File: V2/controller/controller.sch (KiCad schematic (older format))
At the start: 27 parts, among them J0 Molex_PSU_F, J1 4pins_jumper, J2 Flat_7seg_F, J3 Flat_Rpi_Data_F, Q0 BD139-16, Q1 BD139-16, Q2 BD139-16, Q3 BD139-16, Q4 BD139-16, Q5 BD139-16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

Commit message: Solving ERC
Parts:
- removed J0: Molex_PSU_F, symbol Connector:Conn_01x04_Female
- removed J2: Flat_7seg_F, symbol Connector:Conn_01x08_Female
- removed J3: Flat_Rpi_Data_F, symbol Connector:Conn_01x06_Female
- added D0: 1N4007, symbol Device:D
- added J0: Molex_PSU_F, symbol Connector_Generic:Conn_01x04
- added J2: Flat_7seg_F, symbol Connector_Generic:Conn_02x04_Counter_Clockwise
- added J3: Rpi_DATA_F, symbol Connector_Generic:Conn_02x03_Counter_Clockwise
- D1: value LED_RED -> LED_2V_20mA
- R1: value R -> 100R
- gave numbers to parts that had none: 1
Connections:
- net labels added: Earth
- wire segments 122 -> 135
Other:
- moved on the sheet: D1, R1, R10, R11, R12, R13, R9

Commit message: Identify control pins
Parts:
- R1: value 100R -> 150R
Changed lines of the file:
@@
 P 3850 1450
 F 0 "R1" H 3920 1496 50  0000 L CNN
-F 1 "100R" H 3920 1405 50  0000 L CNN
+F 1 "150R" H 3920 1405 50  0000 L CNN
 F 2 "" V 3780 1450 50  0001 C CNN
 F 3 "~" H 3850 1450 50  0001 C CNN

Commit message: Assign footprints
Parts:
- D0: footprint (none) -> Diode_THT:D_A-405_P10.16mm_Horizontal
- D1: footprint (none) -> LED_THT:LED_D5.0mm
- J0: footprint (none) -> PSU:conn_hdd_15-24-4441
- J1: footprint (none) -> Connector_PinHeader_2.00mm:PinHeader_2x02_P2.00mm_Vertical
- J2: footprint (none) -> Connector_PinHeader_2.54mm:PinHeader_2x04_P2.54mm_Horizontal
- J3: footprint (none) -> Connector_PinHeader_2.54mm:PinHeader_2x03_P2.54mm_Horizontal
- Q0, Q1, Q2, Q3, Q4, Q5, Q6: footprint (none) -> Package_TO_SOT_THT:TO-126-3_Vertical
- R0, R1, R10, R11, R12, R13, R2, R3, R4, R5, R6, R7, R8, R9: footprint (none) -> Resistor_THT:R_Axial_DIN0207_L6.3mm_D2.5mm_P10.16mm_Horizontal
- U1: footprint (none) -> Package_DIP:DIP-16_W7.62mm_LongPads
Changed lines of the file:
@@
 F 0 "Q0" H 6991 1596 50  0000 L CNN
 F 1 "BD139-16" H 6991 1505 50  0000 L CNN
-F 2 "" H 7000 1650 50  0001 C CNN
+F 2 "Package_TO_SOT_THT:TO-126-3_Vertical" H 7000 1650 50  0001 C CNN
 F 3 "~" H 6800 1550 50  0001 C CNN
 	1    6800 1550
@@
 F 0 "R1" H 3920 1496 50  0000 L CNN
 F 1 "150R" H 3920 1405 50  0000 L CNN
-F 2 "" V 3780 1450 50  0001 C CNN
+F 2 "Resistor_THT:R_Axial_DIN0207_L6.3mm_D2.5mm_P10.16mm_Horizontal" V 3780 1450 50  0001 C CNN
 F 3 "~" H 3850 1450 50  0001 C CNN
 	1    3850 1450
@@
 F 0 "D1" V 3439 1332 50  0000 R CNN
 F 1 "LED_2V_20mA" V 3348 1332 50  0000 R CNN
-F 2 "" H 3400 1450 50  0001 C CNN
+F 2 "LED_THT:LED_D5.0mm" H 3400 1450 50  0001 C CNN
 F 3 "~" H 3400 1450 50  0001 C CNN
 	1    3400 1450
@@
 F 0 "R2" H 6320 2096 50  0000 L CNN
 F 1 "430R" H 6320 2005 50  0000 L CNN
-F 2 "" V 6180 2050 50  0001 C CNN
+F 2 "Resistor_THT:R_Axial_DIN0207_L6.3mm_D2.5mm_P10.16mm_Horizontal" V 6180 2050 50  0001 C CNN
 F 3 "~" H 6250 2050 50  0001 C CNN
 	1    6250 2050
@@
 F 0 "R0" H 6320 1596 50  0000 L CNN
 F 1 "430R" H 6320 1505 50  0000 L CNN
-F 2 "" V 6180 1550 50  0001 C CNN
+F 2 "Resistor_THT:R_Axial_DIN0207_L6.3mm_D2.5mm_P10.16mm_Horizontal" V 6180 1550 50  0001 C CNN
 F 3 "~" H 6250 1550 50  0001 C CNN
 	1    6250 1550
@@
 F 0 "Q1" H 6991 2096 50  0000 L CNN
 F 1 "BD139-16" H 6991 2005 50  0000 L CNN
-F 2 "" H 7000 2150 50  0001 C CNN
+F 2 "Package_TO_SOT_THT:TO-126-3_Vertical" H 7000 2150 50  0001 C CNN
 F 3 "~" H 6800 2050 50  0001 C CNN
 	1    6800 2050
@@
 F 0 "Q2" H 6991 2596 50  0000 L CNN
 F 1 "BD139-16" H 6991 2505 50  0000 L CNN
-F 2 "" H 7000 2650 50  0001 C CNN
+F 2 "Package_TO_SOT_THT:TO-126-3_Vertical" H 7000 2650 50  0001 C CNN
 F 3 "~" H 6800 2550 50  0001 C CNN
 	1    6800 2550
@@
 F 0 "Q3" H 6991 3096 50  0000 L CNN
 F 1 "BD139-16" H 6991 3005 50  0000 L CNN
-F 2 "" H 7000 3150 50  0001 C CNN
+F 2 "Package_TO_SOT_THT:TO-126-3_Vertical" H 7000 3150 50  0001 C CNN
 F 3 "~" H 6800 3050 50  0001 C CNN
 	1    6800 3050
@@
 F 0 "Q4" H 6991 3596 50  0000 L CNN
 F 1 "BD139-16" H 6991 3505 50  0000 L CNN
-F 2 "" H 7000 3650 50  0001 C CNN
+F 2 "Package_TO_SOT_THT:TO-126-3_Vertical" H 7000 3650 50  0001 C CNN
 F 3 "~" H 6800 3550 50  0001 C CNN
 	1    6800 3550
@@
 F 0 "Q5" H 6991 4096 50  0000 L CNN
 F 1 "BD139-16" H 6991 4005 50  0000 L CNN
-F 2 "" H 7000 4150 50  0001 C CNN
+F 2 "Package_TO_SOT_THT:TO-126-3_Vertical" H 7000 4150 50  0001 C CNN
 F 3 "~" H 6800 4050 50  0001 C CNN
 	1    6800 4050
@@
 F 0 "Q6" H 6991 4596 50  0000 L CNN
 F 1 "BD139-16" H 6991 4505 50  0000 L CNN
-F 2 "" H 7000 4650 50  0001 C CNN
+F 2 "Package_TO_SOT_THT:TO-126-3_Vertical" H 7000 4650 50  0001 C CNN
 F 3 "~" H 6800 4550 50  0001 C CNN
 	1    6800 4550
@@
 F 0 "R3" H 6320 2596 50  0000 L CNN
 F 1 "430R" H 6320 2505 50  0000 L CNN
-F 2 "" V 6180 2550 50  0001 C CNN
+F 2 "Resistor_THT:R_Axial_DIN0207_L6.3mm_D2.5mm_P10.16mm_Horizontal" V 6180 2550 50  0001 C CNN
 F 3 "~" H 6250 2550 50  0001 C CNN
 	1    6250 2550
@@
 F 0 "R4" H 6320 3096 50  0000 L CNN
 F 1 "430R" H 6320 3005 50  0000 L CNN
-F 2 "" V 6180 3050 50  0001 C CNN
+F 2 "Resistor_THT:R_Axial_DIN0207_L6.3mm_D2.5mm_P10.16mm_Horizontal" V 6180 3050 50  0001 C CNN
 F 3 "~" H 6250 3050 50  0001 C CNN
 	1    6250 3050
@@
 F 0 "R5" H 6320 3596 50  0000 L CNN
 F 1 "430R" H 6320 3505 50  0000 L CNN
-F 2 "" V 6180 3550 50  0001 C CNN
+F 2 "Resistor_THT:R_Axial_DIN0207_L6.3mm_D2.5mm_P10.16mm_Horizontal" V 6180 3550 50  0001 C CNN
 F 3 "~" H 6250 3550 50  0001 C CNN
 	1    6250 3550
@@
 F 0 "R6" H 6320 4096 50  0000 L CNN
 F 1 "430R" H 6320 4005 50  0000 L CNN
-F 2 "" V 6180 4050 50  0001 C CNN
+F 2 "Resistor_THT:R_Axial_DIN0207_L6.3mm_D2.5mm_P10.16mm_Horizontal" V 6180 4050 50  0001 C CNN
 F 3 "~" H 6250 4050 50  0001 C CNN
 	1    6250 4050
@@
 F 0 "R7" H 6320 4596 50  0000 L CNN
 F 1 "430R" H 6320 4505 50  0000 L CNN
-F 2 "" V 6180 4550 50  0001 C CNN
+F 2 "Resistor_THT:R_Axial_DIN0207_L6.3mm_D2.5mm_P10.16mm_Horizontal" V 6180 4550 50  0001 C CNN
 F 3 "~" H 6250 4550 50  0001 C CNN
 	1    6250 4550
@@
 F 0 "R8" H 4320 1596 50  0000 L CNN
 F 1 "1k" H 4320 1505 50  0000 L CNN
-F 2 "" V 4180 1550 50  0001 C CNN
+F 2 "Resistor_THT:R_Axial_DIN0207_L6.3mm_D2.5mm_P10.16mm_Horizontal" V 4180 1550 50  0001 C CNN
 F 3 "~" H 4250 1550 50  0001 C CNN
 	1    4250 1550
@@
 F 0 "R9" H 3170 2096 50  0000 L CNN
 F 1 "1k" H 3170 2005 50  0000 L CNN
-F 2 "" V 3030 2050 50  0001 C CNN
+F 2 "Resistor_THT:R_Axial_DIN0207_L6.3mm_D2.5mm_P10.16mm_Horizontal" V 3030 2050 50  0001 C CNN
 F 3 "~" H 3100 2050 50  0001 C CNN
 	1    3100 2050
@@
 F 0 "R10" H 3170 2396 50  0000 L CNN
 F 1 "1k" H 3170 2305 50  0000 L CNN
-F 2 "" V 3030 2350 50  0001 C CNN
+F 2 "Resistor_THT:R_Axial_DIN0207_L6.3mm_D2.5mm_P10.16mm_Horizontal" V 3030 2350 50  0001 C CNN
 F 3 "~" H 3100 2350 50  0001 C CNN
 	1    3100 2350
@@
 F 0 "R11" H 3170 3246 50  0000 L CNN
 F 1 "1k" H 3170 3155 50  0000 L CNN
-F 2 "" V 3030 3200 50  0001 C CNN
+F 2 "Resistor_THT:R_Axial_DIN0207_L6.3mm_D2.5mm_P10.16mm_Horizontal" V 3030 3200 50  0001 C CNN
 F 3 "~" H 3100 3200 50  0001 C CNN
 	1    3100 3200
@@
 F 0 "R12" H 3170 3546 50  0000 L CNN
 F 1 "1k" H 3170 3455 50  0000 L CNN
-F 2 "" V 3030 3500 50  0001 C CNN
+F 2 "Resistor_THT:R_Axial_DIN0207_L6.3mm_D2.5mm_P10.16mm_Horizontal" V 3030 3500 50  0001 C CNN
 F 3 "~" H 3100 3500 50  0001 C CNN
 	1    3100 3500
@@
 F 0 "R13" H 3170 3846 50  0000 L CNN
 F 1 "1k" H 3170 3755 50  0000 L CNN
-F 2 "" V 3030 3800 50  0001 C CNN
+F 2 "Resistor_THT:R_Axial_DIN0207_L6.3mm_D2.5mm_P10.16mm_Horizontal" V 3030 3800 50  0001 C CNN
 F 3 "~" H 3100 3800 50  0001 C CNN
 	1    3100 3800
@@
 F 0 "U1" H 5100 2816 50  0000 C CNN
 F 1 "4511" H 5100 2725 50  0000 C CNN
-F 2 "" H 5100 2250 50  0001 C CNN
+F 2 "Package_DIP:DIP-16_W7.62mm_LongPads" H 5100 2250 50  0001 C CNN
 F 3 "" H 5100 2250 50  0001 C CNN
 	1    5100 2250
@@
 F 0 "J1" H 4000 2867 50  0000 C CNN
 F 1 "4pins_jumper" H 4000 2776 50  0000 C CNN
-F 2 "" H 3950 2650 50  0001 C CNN
+F 2 "Connector_PinHeader_2.00mm:PinHeader_2x02_P2.00mm_Vertical" H 3950 2650 50  0001 C CNN
 F 3 "~" H 3950 2650 50  0001 C CNN
 	1    3950 2650
@@
 F 0 "D0" V 3504 3279 50  0000 L CNN
 F 1 "1N4007" V 3595 3279 50  0000 L CNN
-F 2 "" H 3550 3200 50  0001 C CNN
+F 2 "Diode_THT:D_A-405_P10.16mm_Horizontal" H 3550 3200 50  0001 C CNN
 F 3 "~" H 3550 3200 50  0001 C CNN
 	1    3550 3200
@@
 F 0 "J0" H 1768 1125 50  0000 C CNN
 F 1 "Molex_PSU_F" H 1768 1216 50  0000 C CNN
-F 2 "" H 1850 1550 50  0001 C CNN
+F 2 "PSU:conn_hdd_15-24-4441" H 1850 1550 50  0001 C CNN
 F 3 "~" H 1850 1550 50  0001 C CNN
 	1    1850 1550
@@
 F 0 "J3" H 2000 3067 50  0000 C CNN
 F 1 "Rpi_DATA_F" H 2000 2976 50  0000 C CNN
-F 2 "" H 1950 2750 50  0001 C CNN
+F 2 "Connector_PinHeader_2.54mm:PinHeader_2x03_P2.54mm_Horizontal" H 1950 2750 50  0001 C CNN
 F 3 "~" H 1950 2750 50  0001 C CNN
 	1    1950 2750
@@
 F 0 "J2" H 9000 1667 50  0000 C CNN
 F 1 "Flat_7seg_F" H 9000 1576 50  0000 C CNN
-F 2 "" H 8950 1350 50  0001 C CNN
+F 2 "Connector_PinHeader_2.54mm:PinHeader_2x04_P2.54mm_Horizontal" H 8950 1350 50  0001 C CNN
 F 3 "~" H 8950 1350 50  0001 C CNN
 	1    8950 1350

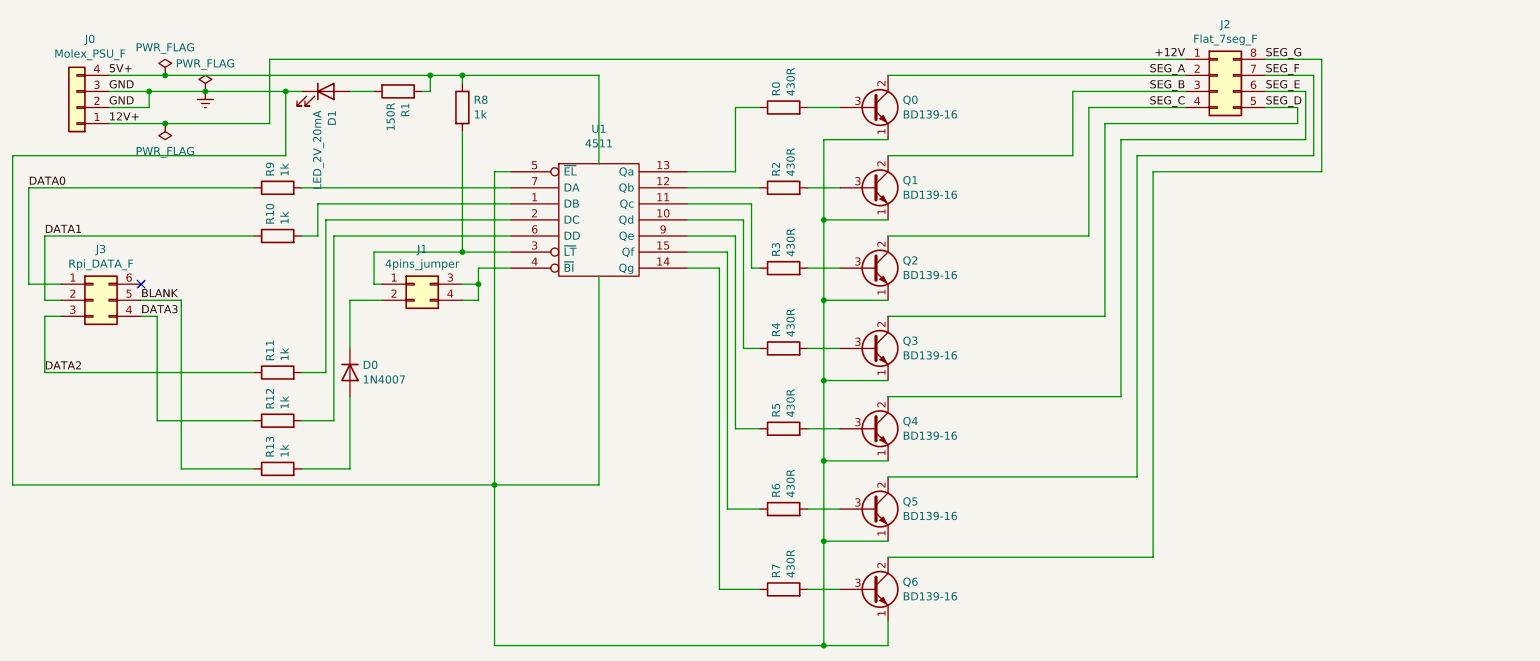
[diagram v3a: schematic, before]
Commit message: swicth for avr
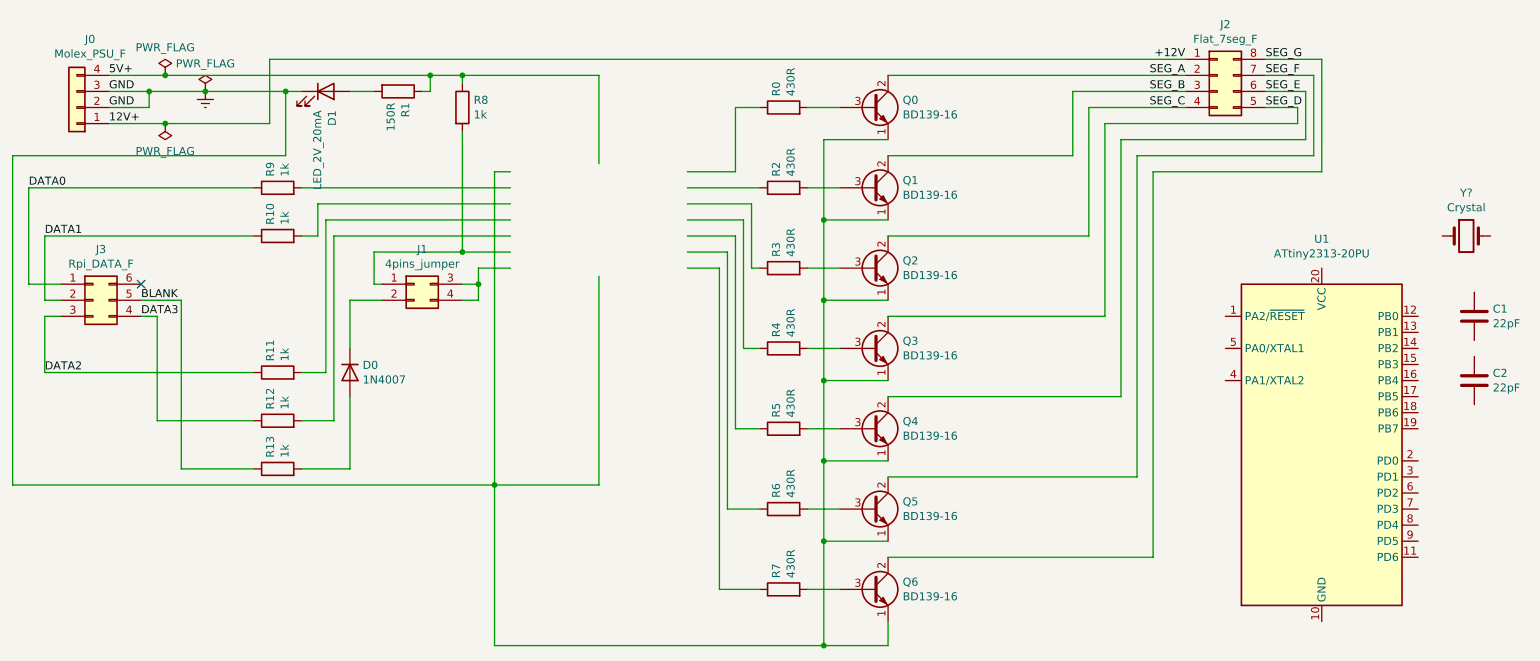
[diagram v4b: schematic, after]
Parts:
- removed U1: 4511, Package_DIP:DIP-16_W7.62mm_LongPads, symbol 4xxx_IEEE:4511
- added C1, C2: 22pF, symbol Device:C
- added U1: ATtiny2313-20PU, Package_DIP:DIP-20_W7.62mm, symbol MCU_Microchip_ATtiny:ATtiny2313-20PU
- added Y?: Crystal, symbol Device:Crystal
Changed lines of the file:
@@
 Wire Wire Line
 	1450 3900 4450 3900
-$Comp
-L 4xxx_IEEE:4511 U1
-U 1 1 5EC72605
-P 5100 2250
-F 0 "U1" H 5100 2816 50  0000 C CNN
-F 1 "4511" H 5100 2725 50  0000 C CNN
-F 2 "Package_DIP:DIP-16_W7.62mm_LongPads" H 5100 2250 50  0001 C CNN
-F 3 "" H 5100 2250 50  0001 C CNN
-	1    5100 2250
-	1    0    0    -1
-$EndComp
 Wire Wire Line
 	4450 4900 6500 4900
@@
 	1    0    0    -1
 $EndComp
+$Comp
+L MCU_Microchip_ATtiny:ATtiny2313-20PU U1
+U 1 1 5F9959D0
+P 9600 3650
+F 0 "U1" H 9600 4931 50  0000 C CNN
+F 1 "ATtiny2313-20PU" H 9600 4840 50  0000 C CNN
+F 2 "Package_DIP:DIP-20_W7.62mm" H 9600 3650 50  0001 C CIN
+F 3 "http://ww1.microchip.com/downloads/en/DeviceDoc/Atmel-2543-AVR-ATtiny2313_Datasheet.pdf" H 9600 3650 50  0001 C CNN
+	1    9600 3650
+	1    0    0    -1
+$EndComp
+$Comp
+L Device:Crystal Y?
+U 1 1 5F9975A7
+P 10500 2350
+F 0 "Y?" H 10500 2618 50  0000 C CNN
+F 1 "Crystal" H 10500 2527 50  0000 C CNN
+F 2 "" H 10500 2350 50  0001 C CNN
+F 3 "~" H 10500 2350 50  0001 C CNN
+	1    10500 2350
+	1    0    0    -1
+$EndComp
+$Comp
+L Device:C C1
+U 1 1 5F9991F2
+P 10550 2850
+F 0 "C1" H 10665 2896 50  0000 L CNN
+F 1 "22pF" H 10665 2805 50  0000 L CNN
+F 2 "" H 10588 2700 50  0001 C CNN
+F 3 "~" H 10550 2850 50  0001 C CNN
+	1    10550 2850
+	1    0    0    -1
+$EndComp
+$Comp
+L Device:C C2
+U 1 1 5F99ADDE
+P 10550 3250
+F 0 "C2" H 10665 3296 50  0000 L CNN
+F 1 "22pF" H 10665 3205 50  0000 L CNN
+F 2 "" H 10588 3100 50  0001 C CNN
+F 3 "~" H 10550 3250 50  0001 C CNN
+	1    10550 3250
+	1    0    0    -1
+$EndComp
